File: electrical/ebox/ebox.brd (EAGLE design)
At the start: 100 x 80 mm, 162 parts, among them IC1 MAX3221CUE, IC10 SN74LVC1G125, IC11 MAX3221CUE, IC12 INA170, IC13 SN74LVC1G125, IC14 SN74LVC1G125, IC15 MAX3221CUE, IC17 SN74LVC1G125, IC18 SN74LVC1G125, IC19 74ALS04D, IC2 LT3652, IC20 AP1509-33, IC24 AP1509-5, IC3 XMEGA128A1, IC4 LT1161, IC5 SN74LVC1G125, IC6 SN74LVC1G125, IC7 MAX3221CUE, IC8 INA170, IC9 SN74LVC1G125, Q1 FDD4141TO252, U1 BLUETOOTH-RN42, U2 D2523T_, X1 BULLET, X10 DEANS, X11 DEANS, X12 7381-2PG-300, X13 B4B-ZR, X14 BULLET, X17 22-23-2021, X18 7381-3PG-300, X19 7381-3PG-300, X2 BULLET, X20 BULLET, X21 BULLET, X22 BULLET, X23 BULLET, X24 B4B-ZR, X3 17984-7PG-300, X4 BULLET, X5 17984-7PG-300, X6 17984-7PG-300, X7 17984-7PG-300, X8 22-23-2031, X9 22-23-2031

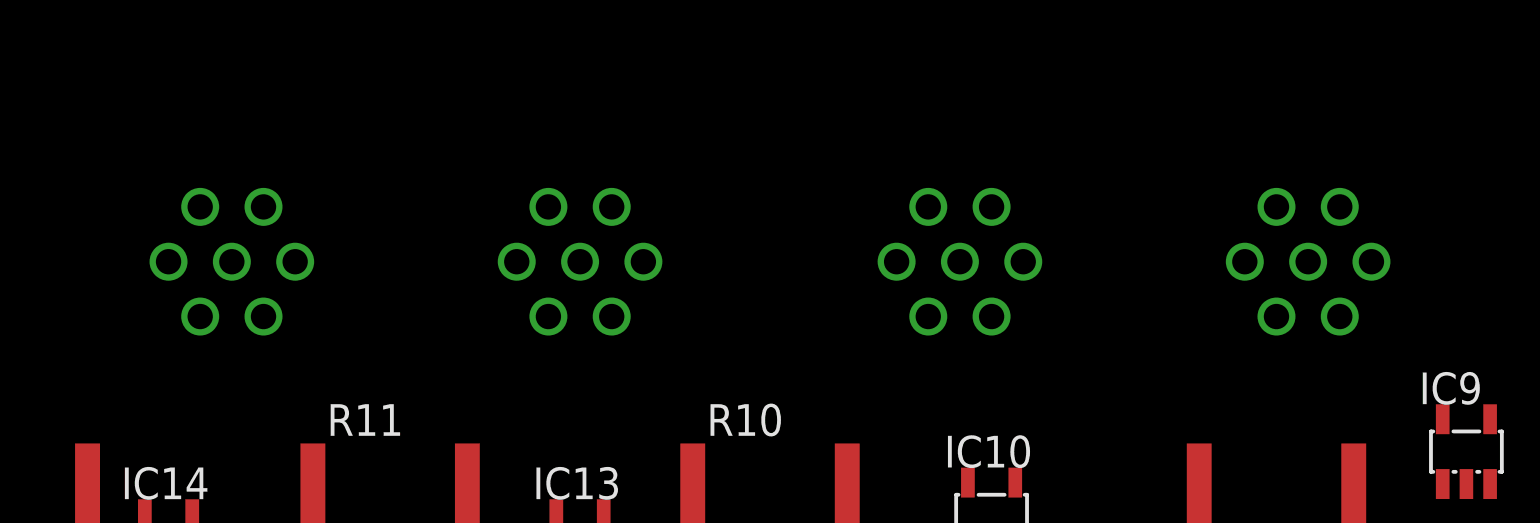
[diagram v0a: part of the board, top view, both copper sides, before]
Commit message: I thought we just committed the changes to the footprints, but apparently we didn't.
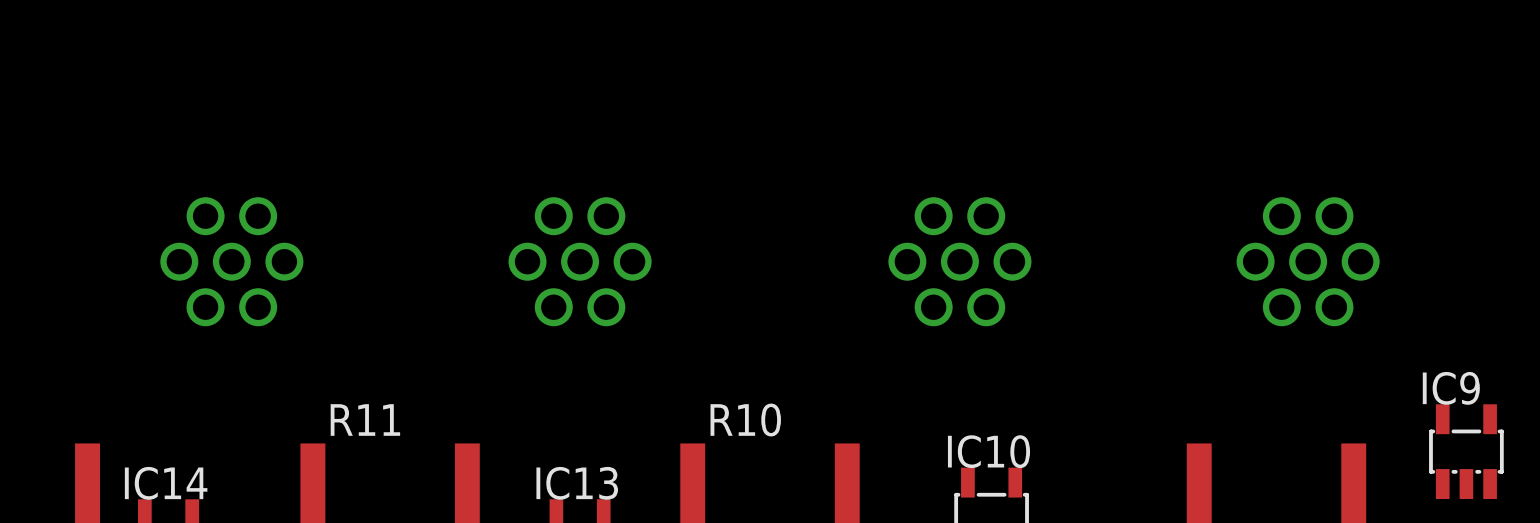
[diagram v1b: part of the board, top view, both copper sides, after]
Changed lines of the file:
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@@
 <contactref element="X3" pad="1"/>
 <contactref element="T2" pad="3"/>
-<wire x1="35.7886" y1="37.3888" x2="44.45" y2="49.53" width="0" layer="19" extent="1-1"/>
+<wire x1="35.7886" y1="37.3888" x2="48.0441" y2="51.356259375" width="0" layer="19" extent="1-1"/>
 </signal>
 <signal name="S1_RX">
@@
 <contactref element="IC1" pad="8"/>
 <contactref element="R16" pad="2"/>
-<wire x1="41.0178" y1="26.405" x2="45.72" y2="51.729640625" width="0" layer="19" extent="1-1"/>
-<wire x1="-105.73" y1="105.41" x2="45.72" y2="51.729640625" width="0" layer="19" extent="1-1"/>
+<wire x1="41.0178" y1="26.405" x2="49.0982" y2="49.53" width="0" layer="19" extent="1-1"/>
+<wire x1="-105.73" y1="105.41" x2="49.0982" y2="49.53" width="0" layer="19" extent="1-1"/>
 </signal>
 <signal name="S1_TX">
@@
 <contactref element="IC1" pad="13"/>
 <contactref element="IC5" pad="4"/>
-<wire x1="35.1822" y1="23.805" x2="48.26" y2="51.729640625" width="0" layer="19" extent="1-1"/>
+<wire x1="35.1822" y1="23.805" x2="48.0441" y2="47.703740625" width="0" layer="19" extent="1-1"/>
 <wire x1="-95.57" y1="62.26" x2="35.1822" y2="23.805" width="0" layer="19" extent="1-1"/>
 </signal>
@@
 <contactref element="PTC9" pad="2"/>
 <contactref element="IC5" pad="5"/>
-<wire x1="-15.088" y1="99.06" x2="49.53" y2="49.53" width="0" layer="19" extent="1-1"/>
+<wire x1="-15.088" y1="99.06" x2="45.9359" y2="47.703740625" width="0" layer="19" extent="1-1"/>
 <wire x1="-97.47" y1="62.26" x2="-15.088" y2="99.06" width="0" layer="19" extent="1-1"/>
 </signal>
@@
 <contactref element="X3" pad="5"/>
 <contactref element="PTC1" pad="2"/>
-<wire x1="-68.428" y1="92.71" x2="48.26" y2="47.330359375" width="0" layer="19" extent="1-1"/>
+<wire x1="-68.428" y1="92.71" x2="44.8818" y2="49.53" width="0" layer="19" extent="1-1"/>
 </signal>
 <signal name="S1_GPIO_B">
 <contactref element="X3" pad="6"/>
 <contactref element="PTC2" pad="2"/>
-<wire x1="-76.048" y1="92.71" x2="45.72" y2="47.330359375" width="0" layer="19" extent="1-1"/>
+<wire x1="-76.048" y1="92.71" x2="45.9359" y2="51.356259375" width="0" layer="19" extent="1-1"/>
 </signal>
 <signal name="S2_RX">
@@
 <contactref element="IC7" pad="8"/>
 <contactref element="R17" pad="2"/>
-<wire x1="86.7378" y1="26.405" x2="88.9" y2="51.729640625" width="0" layer="19" extent="1-1"/>
-<wire x1="-112.08" y1="105.41" x2="88.9" y2="51.729640625" width="0" layer="19" extent="1-1"/>
+<wire x1="86.7378" y1="26.405" x2="92.2782" y2="49.53" width="0" layer="19" extent="1-1"/>
+<wire x1="-112.08" y1="105.41" x2="92.2782" y2="49.53" width="0" layer="19" extent="1-1"/>
 </signal>
 <signal name="S2_12V">
 <contactref element="X5" pad="1"/>
 <contactref element="T3" pad="3"/>
-<wire x1="86.5886" y1="37.3888" x2="87.63" y2="49.53" width="0" layer="19" extent="1-1"/>
+<wire x1="86.5886" y1="37.3888" x2="91.2241" y2="51.356259375" width="0" layer="19" extent="1-1"/>
 </signal>
 <signal name="S2_TX">
@@
 <contactref element="IC7" pad="13"/>
 <contactref element="IC9" pad="4"/>
-<wire x1="97.47" y1="43.21" x2="91.44" y2="51.729640625" width="0" layer="19" extent="1-1"/>
+<wire x1="97.47" y1="43.21" x2="91.2241" y2="47.703740625" width="0" layer="19" extent="1-1"/>
 <wire x1="80.9022" y1="23.805" x2="97.47" y2="43.21" width="0" layer="19" extent="1-1"/>
 </signal>
@@
 <contactref element="PTC10" pad="2"/>
 <contactref element="IC9" pad="5"/>
-<wire x1="95.57" y1="43.21" x2="92.71" y2="49.53" width="0" layer="19" extent="1-1"/>
-<wire x1="-45.568" y1="92.71" x2="92.71" y2="49.53" width="0" layer="19" extent="1-1"/>
+<wire x1="95.57" y1="43.21" x2="89.1159" y2="47.703740625" width="0" layer="19" extent="1-1"/>
+<wire x1="-45.568" y1="92.71" x2="89.1159" y2="47.703740625" width="0" layer="19" extent="1-1"/>
 </signal>
 <signal name="S3_12V">
 <contactref element="X6" pad="1"/>
 <contactref element="T4" pad="3"/>
-<wire x1="66.2686" y1="37.3888" x2="73.66" y2="49.53" width="0" layer="19" extent="1-1"/>
+<wire x1="66.2686" y1="37.3888" x2="77.2541" y2="51.356259375" width="0" layer="19" extent="1-1"/>
 </signal>
 <signal name="S3_RX">
@@
 <contactref element="IC11" pad="8"/>
 <contactref element="R18" pad="2"/>
-<wire x1="62.6078" y1="26.405" x2="74.93" y2="51.729640625" width="0" layer="19" extent="1-1"/>
+<wire x1="62.6078" y1="26.405" x2="78.3082" y2="49.53" width="0" layer="19" extent="1-1"/>
 <wire x1="-118.43" y1="105.41" x2="62.6078" y2="26.405" width="0" layer="19" extent="1-1"/>
 </signal>
@@
 <contactref element="IC11" pad="13"/>
 <contactref element="IC13" pad="4"/>
-<wire x1="61.91" y1="39.4" x2="77.47" y2="51.729640625" width="0" layer="19" extent="1-1"/>
+<wire x1="61.91" y1="39.4" x2="77.2541" y2="47.703740625" width="0" layer="19" extent="1-1"/>
 <wire x1="56.7722" y1="23.805" x2="61.91" y2="39.4" width="0" layer="19" extent="1-1"/>
 </signal>
@@
 <contactref element="IC13" pad="5"/>
 <contactref element="PTC11" pad="2"/>
-<wire x1="60.01" y1="39.4" x2="78.74" y2="49.53" width="0" layer="19" extent="1-1"/>
+<wire x1="60.01" y1="39.4" x2="75.1459" y2="47.703740625" width="0" layer="19" extent="1-1"/>
 <wire x1="-53.188" y1="92.71" x2="60.01" y2="39.4" width="0" layer="19" extent="1-1"/>
 </signal>
@@
 <contactref element="X7" pad="1"/>
 <contactref element="T5" pad="3"/>
-<wire x1="51.0286" y1="37.3888" x2="58.42" y2="49.53" width="0" layer="19" extent="1-1"/>
+<wire x1="51.0286" y1="37.3888" x2="62.0141" y2="51.356259375" width="0" layer="19" extent="1-1"/>
 </signal>
 <signal name="S4_RX">
@@
 <contactref element="IC15" pad="8"/>
 <contactref element="R19" pad="2"/>
-<wire x1="29.5878" y1="40.375" x2="59.69" y2="51.729640625" width="0" layer="19" extent="1-1"/>
+<wire x1="29.5878" y1="40.375" x2="63.0682" y2="49.53" width="0" layer="19" extent="1-1"/>
 <wire x1="-15.56" y1="111.76" x2="29.5878" y2="40.375" width="0" layer="19" extent="1-1"/>
 </signal>
@@
 <contactref element="IC15" pad="13"/>
 <contactref element="IC17" pad="4"/>
-<wire x1="35.24" y1="50.83" x2="62.23" y2="51.729640625" width="0" layer="19" extent="1-1"/>
+<wire x1="35.24" y1="50.83" x2="62.0141" y2="47.703740625" width="0" layer="19" extent="1-1"/>
 <wire x1="23.7522" y1="37.775" x2="35.24" y2="50.83" width="0" layer="19" extent="1-1"/>
 </signal>
@@
 <contactref element="IC17" pad="5"/>
 <contactref element="PTC12" pad="2"/>
-<wire x1="33.34" y1="50.83" x2="63.5" y2="49.53" width="0" layer="19" extent="1-1"/>
+<wire x1="33.34" y1="50.83" x2="59.9059" y2="47.703740625" width="0" layer="19" extent="1-1"/>
 <wire x1="-60.808" y1="92.71" x2="33.34" y2="50.83" width="0" layer="19" extent="1-1"/>
 </signal>
@@
 <contactref element="X7" pad="5"/>
 <contactref element="PTC7" pad="2"/>
-<wire x1="-114.148" y1="92.71" x2="62.23" y2="47.330359375" width="0" layer="19" extent="1-1"/>
+<wire x1="-114.148" y1="92.71" x2="58.8518" y2="49.53" width="0" layer="19" extent="1-1"/>
 </signal>
 <signal name="S4_GPIO_B">
 <contactref element="X7" pad="6"/>
 <contactref element="PTC8" pad="2"/>
-<wire x1="-121.768" y1="92.71" x2="59.69" y2="47.330359375" width="0" layer="19" extent="1-1"/>
+<wire x1="-121.768" y1="92.71" x2="59.9059" y2="51.356259375" width="0" layer="19" extent="1-1"/>
 </signal>
 <signal name="N$1">
@@
 <contactref element="PTC3" pad="2"/>
 <contactref element="X5" pad="5"/>
-<wire x1="-83.668" y1="92.71" x2="91.44" y2="47.330359375" width="0" layer="19" extent="1-1"/>
+<wire x1="-83.668" y1="92.71" x2="88.0618" y2="49.53" width="0" layer="19" extent="1-1"/>
 </signal>
 <signal name="S2_GPIO_B">
 <contactref element="PTC4" pad="2"/>
 <contactref element="X5" pad="6"/>
-<wire x1="-91.288" y1="92.71" x2="88.9" y2="47.330359375" width="0" layer="19" extent="1-1"/>
+<wire x1="-91.288" y1="92.71" x2="89.1159" y2="51.356259375" width="0" layer="19" extent="1-1"/>
 </signal>
 <signal name="S1_RX_33V">
@@
 <contactref element="PTC5" pad="2"/>
 <contactref element="X6" pad="5"/>
-<wire x1="-98.908" y1="92.71" x2="77.47" y2="47.330359375" width="0" layer="19" extent="1-1"/>
+<wire x1="-98.908" y1="92.71" x2="74.0918" y2="49.53" width="0" layer="19" extent="1-1"/>
 </signal>
 <signal name="S3_GPIO_B">
 <contactref element="PTC6" pad="2"/>
 <contactref element="X6" pad="6"/>
-<wire x1="-106.528" y1="92.71" x2="74.93" y2="47.330359375" width="0" layer="19" extent="1-1"/>
+<wire x1="-106.528" y1="92.71" x2="75.1459" y2="51.356259375" width="0" layer="19" extent="1-1"/>
 </signal>
 <signal name="N$40">
